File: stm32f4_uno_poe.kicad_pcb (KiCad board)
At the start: 2 copper layers, 68.6 x 53.3 mm, 94 parts, among them J104 STM32 GPIO, J106 Power, J107 Conn_01x04, J108 Ethernet, J111 Analog, J112 Barrel_Jack, J113 Conn_01x02, Q201 Si7450DP, U201 TCMT1107, U202 CJ431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

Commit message: WIP
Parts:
- removed R220: 200, Resistor_SMD:R_0402_1005Metric
- R218: footprint Resistor_SMD:R_0402_1005Metric -> Resistor_SMD:R_0603_1608Metric
- R219: value 4k7 -> 4k99; footprint Resistor_SMD:R_0402_1005Metric -> Resistor_SMD:R_0603_1608Metric
- moved R218 1.53 mm to (174.9, 83.0)
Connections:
- R219 pad 1: Net-(R219-Pad1) -> /PoE/VDD

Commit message: WIP
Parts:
- D202: value SS210 -> SS220
- D205: value 1A 200V 35ns -> 1A 1kV 75ns
- R218: value 20k -> 10k
- R219: value 4k99 -> 15k
- U201: value TCMT1107 -> EL3H7(A)(TA)-G
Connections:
- U201 pad 1: /PoE/CTL -> Net-(R201-Pad2)
- U201 pad 2: /PoE/PGND -> Net-(D201-A)
- U201 pad 3: Net-(D201-A) -> /PoE/PGND
- U201 pad 4: Net-(R201-Pad2) -> /PoE/CTL
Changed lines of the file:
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@@
     (property "Sheetfile" "poe.kicad_sch")
     (property "Sheetname" "PoE")
-    (property "isBasicPart" "NO")
+    (property "isBasicPart" "YES")
     (property "ki_description" "Diode, small symbol")
     (property "ki_keywords" "diode")
@@
     (descr "Diode SMA (DO-214AC)")
     (tags "Diode SMA (DO-214AC)")
-    (property "Description" "1V@1A 35ns Single 1A 200V SMA  Diodes - Fast Recovery Rectifiers ROHS")
-    (property "JLCPCB Part #" "C116492")
-    (property "Manufacturer" "Shandong Jingdao Microelectronics")
-    (property "Partnumber" "ES1D")
+    (property "Description" "1.7V@1A 75ns Single 1A 1kV SMA  Diodes - Fast Recovery Rectifiers ROHS")
+    (property "JLCPCB Part #" "C412437")
+    (property "Manufacturer" "MDD")
+    (property "Partnumber" "US1M")
     (property "Sheetfile" "poe.kicad_sch")
     (property "Sheetname" "PoE")
-    (property "isBasicPart" "NO")
+    (property "isBasicPart" "YES")
     (property "ki_description" "Diode, small symbol")
     (property "ki_keywords" "diode")
@@
         (effects (font (size 1 1) (thickness 0.15)))
     )
-    (fp_text value "1A 200V 35ns" (at 0 2.6) (layer "F.Fab") hide
+    (fp_text value "1A 1kV 75ns" (at 0 2.6) (layer "F.Fab") hide
         (effects (font (size 1 1) (thickness 0.15)))
     )
@@
     (descr "SOP, 4 Pin (http://www.vishay.com/docs/83510/tcmt1100.pdf), generated with kicad-footprint-generator ipc_gullwing_generator.py")
     (tags "SOP SO")
+    (property "Description" "80V 3750V 50mA 0.1V@1mA,10mA 1 6V 1.2V DC SOP-4-1.27mm  Optocouplers - Phototransistor Output ROHS")
+    (property "JLCPCB Part #" "C181879")
+    (property "Manufacturer" "Everlight Elec")
+    (property "Partnumber" "EL3H7(A)(TA)-G")
     (property "Sheetfile" "poe.kicad_sch")
     (property "Sheetname" "PoE")
+    (property "isBasicPart" "NO")
     (property "ki_description" "Optocoupler, Vce 70V, CTR 80-160%, Viso 3750V (RMS), SOP-4")
     (property "ki_keywords" "NPN DC opto")
@@
         (effects (font (size 0.8 0.8) (thickness 0.15)))
     )
-    (fp_text value "TCMT1107" (at 0 2.25) (layer "F.Fab") hide
+    (fp_text value "EL3H7(A)(TA)-G" (at 0 2.25) (layer "F.Fab") hide
         (effects (font (size 0.8 0.8) (thickness 0.15)))
     )
@@
       (stroke (width 0.1) (type solid)) (layer "F.Fab"))
     (pad "1" smd roundrect (at -3.1875 -0.635) (size 1.625 0.6) (layers "F.Cu" "F.Paste" "F.Mask") (roundrect_rratio 0.25)
-      (net 29 "/PoE/CTL") (pintype "passive"))
+      (net 50 "Net-(R201-Pad2)") (pintype "passive"))
     (pad "2" smd roundrect (at -3.1875 0.635) (size 1.625 0.6) (layers "F.Cu" "F.Paste" "F.Mask") (roundrect_rratio 0.25)
-      (net 33 "/PoE/PGND") (pintype "passive"))
-    (pad "3" smd roundrect (at 3.1875 0.635) (size 1.625 0.6) (layers "F.Cu" "F.Paste" "F.Mask") (roundrect_rratio 0.25)
       (net 35 "Net-(D201-A)") (pintype "passive"))
+    (pad "3" smd roundrect (at 3.1875 0.635) (size 1.625 0.6) (layers "F.Cu" "F.Paste" "F.Mask") (roundrect_rratio 0.25)
+      (net 33 "/PoE/PGND") (pintype "passive"))
     (pad "4" smd roundrect (at 3.1875 -0.635) (size 1.625 0.6) (layers "F.Cu" "F.Paste" "F.Mask") (roundrect_rratio 0.25)
-      (net 50 "Net-(R201-Pad2)") (pintype "passive"))
+      (net 29 "/PoE/CTL") (pintype "passive"))
     (model "${KICAD6_3DMODEL_DIR}/Package_SO.3dshapes/SOP-4_4.4x2.6mm_P1.27mm.wrl"
       (offset (xyz 0 0 0))
@@
     (property "ki_keywords" "connector")
     (attr through_hole exclude_from_bom)
-    (fp_text reference "J113" (at 0 -2.33) (layer "F.SilkS")
+    (fp_text reference "J113" (at 0 -2.33) (layer "F.SilkS") hide
         (effects (font (size 1 1) (thickness 0.15)))
     )
-    (fp_text value "Conn_01x02" (at 0 4.87) (layer "F.Fab")
+    (fp_text value "Conn_01x02" (at 0 4.87) (layer "F.Fab") hide
         (effects (font (size 1 1) (thickness 0.15)))
     )
@@
     (descr "Resistor SMD 0603 (1608 Metric), square (rectangular) end terminal, IPC_7351 nominal, (Body size source: IPC-SM-782 page 72, https://www.pcb-3d.com/wordpress/wp-content/uploads/ipc-sm-782a_amendment_1_and_2.pdf), generated with kicad-footprint-generator")
     (tags "resistor")
-    (property "Description" "100mW Thick Film Resistors ±100ppm/℃ ±1% 20kΩ 0603  Chip Resistor - Surface Mount ROHS")
-    (property "JLCPCB Part #" "C4184")
+    (property "Description" "100mW Thick Film Resistors ±100ppm/℃ ±1% 10kΩ 0603  Chip Resistor - Surface Mount ROHS")
+    (property "JLCPCB Part #" "C25804")
     (property "Manufacturer" "UNI-ROYAL(Uniroyal Elec)")
-    (property "Partnumber" "0603WAF2002T5E")
+    (property "Partnumber" "0603WAF1002T5E")
     (property "Sheetfile" "poe.kicad_sch")
     (property "Sheetname" "PoE")
@@
     (property "ki_keywords" "R resistor")
     (attr smd)
-    (fp_text reference "R218" (at 0 -1.43 180) (layer "F.SilkS")
+    (fp_text reference "R218" (at 0 -1.43 180) (layer "F.SilkS") hide
         (effects (font (size 1 1) (thickness 0.15)))
     )
-    (fp_text value "20k" (at 0 1.43 180) (layer "F.Fab")
+    (fp_text value "10k" (at 0 1.43 180) (layer "F.Fab") hide
         (effects (font (size 1 1) (thickness 0.15)))
     )
@@
     (property "ki_keywords" "DC power barrel jack connector")
     (attr through_hole exclude_from_bom)
-    (fp_text reference "J112" (at 5.75 8.45) (layer "F.SilkS")
+    (fp_text reference "J112" (at 5.75 8.45) (layer "F.SilkS") hide
         (effects (font (size 1 1) (thickness 0.15)))
     )
-    (fp_text value "Barrel_Jack" (at -5.5 6.2) (layer "F.Fab")
+    (fp_text value "Barrel_Jack" (at -5.5 6.2) (layer "F.Fab") hide
         (effects (font (size 1 1) (thickness 0.15)))
     )
@@
     (descr "SOT, 3 Pin (https://www.jedec.org/system/files/docs/to-236h.pdf variant AB), generated with kicad-footprint-generator ipc_gullwing_generator.py")
     (tags "SOT TO_SOT_SMD")
+    (property "Description" "30V Dual 200mA 0.4V@10mA SOT-23(TO-236)  Schottky Barrier Diodes (SBD) ROHS")
+    (property "JLCPCB Part #" "C7420333")
+    (property "Manufacturer" "hongjiacheng")
+    (property "Partnumber" "BAT54S")
     (property "Sheetfile" "poe.kicad_sch")
     (property "Sheetname" "PoE")
+    (property "isBasicPart" "YES")
     (property "ki_description" "Vr 30V, If 200mA, Dual schottky barrier diode, in series, SOT-323")
     (property "ki_keywords" "schottky diode")
@@
     (property "Sheetfile" "poe.kicad_sch")
     (property "Sheetname" "PoE")
-    (property "isBasicPart" "NO")
+    (property "isBasicPart" "YES")
     (property "ki_description" "Diode, small symbol")
     (property "ki_keywords" "diode")
@@
     (property "ki_keywords" "PCB Flyback Transformer")
     (attr smd)
-    (fp_text reference "TR201" (at 0 -8.255 90) (layer "F.SilkS")
+    (fp_text reference "TR201" (at 0 -8.255 90) (layer "F.SilkS") hide
         (effects (font (size 1 1) (thickness 0.15)))
     )
-    (fp_text value "Coilcraft POE40Q-xxE" (at 0.254 6.595 90) (layer "F.Fab")
+    (fp_text value "Coilcraft POE40Q-xxE" (at 0.254 6.595 90) (layer "F.Fab") hide
         (effects (font (size 1 1) (thickness 0.15)))
     )
@@
     (descr "Diode SMA (DO-214AC)")
     (tags "Diode SMA (DO-214AC)")
-    (property "Description" "100V 850mV@2A 2A SMA(DO-214AC)  Schottky Barrier Diodes (SBD) ROHS")
-    (property "JLCPCB Part #" "C14996")
+    (property "Description" "200V Single 0.95V@2.0A 2A SMA  Schottky Barrier Diodes (SBD) ROHS")
+    (property "JLCPCB Part #" "C7420361")
     (property "Manufacturer" "MDD")
-    (property "Manufacturer_Name" "MDD")
-    (property "Manufacturer_Part_Number" "SS210")
     (property "Partnumber" "SS210")
     (property "Sheetfile" "poe.kicad_sch")
@@
         (effects (font (size 0.8 0.8) (thickness 0.15)))
     )
-    (fp_text value "SS210" (at 0 2.6 90) (layer "F.Fab") hide
+    (fp_text value "SS220" (at 0 2.6 90) (layer "F.Fab") hide
         (effects (font (size 0.8 0.8) (thickness 0.15)))
     )
@@
     (descr "Resistor SMD 0603 (1608 Metric), square (rectangular) end terminal, IPC_7351 nominal, (Body size source: IPC-SM-782 page 72, https://www.pcb-3d.com/wordpress/wp-content/uploads/ipc-sm-782a_amendment_1_and_2.pdf), generated with kicad-footprint-generator")
     (tags "resistor")
-    (property "Description" "100mW Thick Film Resistors ±100ppm/℃ ±1% 4.99kΩ 0603  Chip Resistor - Surface Mount ROHS")
-    (property "JLCPCB Part #" "C23046")
+    (property "Description" "100mW Thick Film Resistors ±100ppm/℃ ±1% 15kΩ 0603  Chip Resistor - Surface Mount ROHS")
+    (property "JLCPCB Part #" "C22809")
     (property "Manufacturer" "UNI-ROYAL(Uniroyal Elec)")
-    (property "Partnumber" "0603WAF4991T5E")
+    (property "Partnumber" "0603WAF1502T5E")
     (property "Sheetfile" "poe.kicad_sch")
     (property "Sheetname" "PoE")
@@
     (property "ki_keywords" "R resistor")
     (attr smd)
-    (fp_text reference "R219" (at 0 -1.43 180) (layer "F.SilkS")
+    (fp_text reference "R219" (at 0 -1.43 180) (layer "F.SilkS") hide
         (effects (font (size 1 1) (thickness 0.15)))
     )
-    (fp_text value "4k99" (at 0 1.43 180) (layer "F.Fab")
+    (fp_text value "15k" (at 0 1.43 180) (layer "F.Fab") hide
         (effects (font (size 1 1) (thickness 0.15)))
     )

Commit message: WIP
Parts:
- removed C208, C212: 1n 2kV, Capacitor_SMD:C_1206_3216Metric
- added D209: 58V TVS, Diode_SMD:D_SMB, F.Cu at (119.0, 64.1)
- added J102: Digital/PWM, Connector_PinSocket_2.54mm:PinSocket_1x10_P2.54mm_Vertical, F.Cu at (118.8, 49.2)
- added J109: Digital/PWM, Connector_PinSocket_2.54mm:PinSocket_1x08_P2.54mm_Vertical, F.Cu at (145.7, 49.2)
- added R220: 470, Resistor_SMD:R_0402_1005Metric, F.Cu at (134.5, 57.3)
- added TP201: VDD, TestPoint:TestPoint_THTPad_2.0x2.0mm_Drill1.0mm, F.Cu at (105.5, 49.7)
- added TP202: VSS, TestPoint:TestPoint_THTPad_2.0x2.0mm_Drill1.0mm, F.Cu at (102.3, 49.7)
- D214: value 64V TVS -> 58V TVS; footprint Diode_SMD:D_SMC -> Diode_SMD:D_SMA
- L201, L202, L203, L204: value 100Ω@100MHz (800mA) -> 600Ω@100MHz (500mA)
- R215: value 1k -> 470; footprint Resistor_SMD:R_0805_2012Metric -> Resistor_SMD:R_0402_1005Metric
- R217: value 68 -> 330; footprint Resistor_SMD:R_0805_2012Metric -> Resistor_SMD:R_0402_1005Metric
- moved R231 121.6 mm to (129.6, 118.7)
- moved C219 121.0 mm to (132.9, 118.4)
- moved U204 114.0 mm to (129.6, 121.7)
- moved D207 108.3 mm to (128.7, 83.6), turned to -135 degrees
- moved R228 100.6 mm to (126.6, 87.3)
- moved D214 94.5 mm to (109.3, 51.6), turned to -90 degrees
- moved L205 93.9 mm to (116.6, 70.2)
- moved R221 90.0 mm to (116.6, 78.5), turned to 180 degrees
- moved C214 88.6 mm to (116.6, 76.3), turned to 180 degrees
- moved C207 87.0 mm to (103.7, 75.7)
- moved D205 85.6 mm to (110.4, 77.3), turned to -90 degrees
- moved C211 84.1 mm to (106.5, 68.2)
- moved R227 83.7 mm to (121.0, 88.1), turned to -90 degrees
- moved C221 79.3 mm to (142.5, 65.1)
- moved C217 79.3 mm to (142.5, 57.3)
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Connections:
- net Net-(C213-Pad1) renamed /PoE/VDD_PRI+
- net Net-(D205-A) renamed /PoE/VDD_PRI-
- net Net-(D205-K) renamed /PoE/VDD_SN
- J106 pad 8: /V_{IN} -> /PoE/24V
- R215 pad 1: /PoE/VSS -> Net-(R215-Pad1)
- R215 pad 2: Net-(U203-CLS) -> Net-(R215-Pad2)
- R217 pad 1: /PoE/VSS -> Net-(R215-Pad2)
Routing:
- net /PoE/CTL: track 0.00 -> 15.0 mm
- net /PoE/VB: track 0.00 -> 14.3 mm
- net /PoE/V_{AUX}-: track 12.2 -> 0.00 mm
- net /PoE/VDD_PRI-: track 0.00 -> 11.4 mm
- net /PoE/V_{AUX}+: track 8.04 -> 0.00 mm
- net /PoE/APD: track 0.00 -> 6.28 mm
- net /PoE/AUX: track 5.56 -> 0.00 mm
- net /PoE/FRS: track 0.00 -> 4.14 mm
- net /PoE/BLNK: track 0.00 -> 3.78 mm
- net /PoE/PGND: track 2.80 -> 0.00 mm, vias 0 -> 4
- net Net-(C202-Pad2): track 0.00 -> 1.54 mm
- net Net-(R208-Pad1): track 0.00 -> 1.49 mm
- net GND: vias 0 -> 1
- added copper zone on B.Cu, net /PoE/PGND
- added copper zone on F.Cu, net /PoE/PGND
- added copper zone on F.Cu, net GND

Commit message: WIP
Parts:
- moved R224 21.1 mm to (116.1, 70.2), turned to 90 degrees
- moved R225 19.6 mm to (114.5, 70.2), turned to 90 degrees
- moved R231 19.2 mm to (111.0, 114.0)
- moved U204 19.2 mm to (111.0, 117.0)
- moved C219 19.2 mm to (114.3, 113.7)
- moved R204 18.7 mm to (179.1, 83.1)
- moved R207 18.7 mm to (177.6, 83.1)
- moved R213 18.7 mm to (176.1, 83.1)
- moved R214 18.7 mm to (174.5, 83.1)
- moved R216 18.7 mm to (173.0, 83.1)
- moved C205 18.7 mm to (181.5, 79.8)
- moved U202 18.7 mm to (175.3, 79.8)
- moved C206 18.7 mm to (178.5, 79.8)
- moved R212 18.7 mm to (180.0, 79.8)
- moved C209 16.4 mm to (115.5, 64.1), turned to -90 degrees
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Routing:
- net /PoE/VDD: track 0.00 -> 93.8 mm, vias 0 -> 2
- net /PoE/VSS: track 0.00 -> 75.9 mm
- net Net-(Q201-S-Pad1): track 0.00 -> 41.3 mm
- net /PoE/AUX: track 0.00 -> 38.4 mm, vias 0 -> 2
- net Net-(D206-A): track 0.00 -> 36.7 mm, vias 0 -> 2
- net /PoE/VC: track 0.00 -> 36.0 mm
- net /PoE/VDD_PRI+: track 0.00 -> 30.1 mm, vias 0 -> 3
- net /PoE/V_{AUX}+: track 0.00 -> 25.6 mm
- net /PoE/CS: track 0.00 -> 19.1 mm
- net /PoE/VDD_B: track 0.00 -> 12.5 mm
- net /PoE/VSS_B: track 0.00 -> 12.4 mm
- net /PoE/VDD_PRI-: track 11.4 -> 0.00 mm, vias 0 -> 13
- net /PoE/V_{AUX}-: track 0.00 -> 10.6 mm
- net /PoE/GATE: track 0.00 -> 8.54 mm
- net /PoE/PR78: track 0.00 -> 8.18 mm
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- added copper zone on B.Cu, net /PoE/VDD_PRI+
- added copper zone on B.Cu, net /PoE/VDD_PRI-
- added copper zone on F.Cu, net /PoE/VDD_PRI-

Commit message: PCB ready
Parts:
- removed J102: Digital/PWM, Connector_PinSocket_2.54mm:PinSocket_1x10_P2.54mm_Vertical
- removed J104: STM32 GPIO, Connector_PinSocket_2.54mm:PinSocket_1x08_P2.54mm_Vertical
- removed J108: Ethernet, Connector_PinSocket_2.54mm:PinSocket_1x10_P2.54mm_Vertical
- removed J109: Digital/PWM, Connector_PinSocket_2.54mm:PinSocket_1x08_P2.54mm_Vertical
- removed J111: Analog, Connector_PinSocket_2.54mm:PinSocket_1x06_P2.54mm_Vertical
- removed R231: 10k, Resistor_SMD:R_0603_1608Metric
- removed U204: EL357N(C)(TA)-G, Package_SO:SOP-4_3.8x4.1mm_P2.54mm
- added D210: LED green, LED_SMD:LED_0603_1608Metric, F.Cu at (165.5, 77.4)
- added R232: 4k7, Resistor_SMD:R_0402_1005Metric, F.Cu at (165.4, 78.9)
- TR201: value Coilcraft POE40Q-xxE -> Coilcraft POE40Q-24E
- moved C206 35.4 mm to (150.5, 58.1)
- moved R212 35.4 mm to (152.1, 58.1)
- moved C205 35.4 mm to (153.6, 58.1), turned to 90 degrees
- moved U202 35.3 mm to (147.5, 58.1)
- moved R213 30.5 mm to (158.5, 58.1)
- moved R214 30.5 mm to (157.0, 58.1)
- moved R216 30.5 mm to (155.5, 58.1)
- moved R207 30.3 mm to (160.5, 58.1)
- moved R204 30.3 mm to (162.0, 58.1)
- moved C219 28.2 mm to (131.0, 91.0), turned to -90 degrees
- moved C225 8.81 mm to (126.8, 68.5)
- moved D201 3.94 mm to (148.6, 66.5)
- moved C201 3.68 mm to (148.6, 63.2), turned to 180 degrees
- moved R202 3.68 mm to (148.6, 61.4), turned to 180 degrees
- moved R201 3.17 mm to (148.6, 70.0)
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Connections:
- net /PoE/24V renamed /PoE/+24V
- net Net-(D208-A-Pad1) renamed /PoE/+V_SEC
- net Net-(Q201-S-Pad1) renamed /PoE/PGND_S
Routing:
- net /PoE/+24V: track 0.00 -> 94.8 mm, vias 0 -> 5
- net /PoE/T2P: track 0.00 -> 42.4 mm, vias 0 -> 2
- net /PoE/VC: track 36.0 -> 73.1 mm, vias 0 -> 3
- net Net-(D201-A): track 0.00 -> 29.8 mm
- net Net-(U202-REF): track 0.00 -> 17.7 mm
- net Net-(C222-Pad2): track 0.00 -> 4.73 mm
- net Net-(D201-COM): track 0.00 -> 4.59 mm
- net Net-(R201-Pad2): track 0.00 -> 3.40 mm
- net /PoE/VB: track 21.5 -> 23.9 mm
- net Net-(D210-A): track 0.00 -> 1.69 mm
- net Net-(C206-Pad2): track 0.00 -> 1.54 mm
- net Net-(R214-Pad2): track 0.00 -> 1.52 mm
- net Net-(R213-Pad2): track 0.00 -> 1.52 mm
- net /PoE/CTL: track 13.1 -> 14.4 mm
- net /PoE/VDD: track 93.8 -> 92.9 mm
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- added copper zone on B.Cu, net /PoE/+24V
- added copper zone on F.Cu, net /PoE/+24V
- added copper zone on B.Cu, net /PoE/+V_SEC
- added copper zone on F.Cu, net /PoE/+V_SEC

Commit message: #2 Add silkscreen texts
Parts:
- added G***: LOGO, #Logo:e-Logo 5mm, F.Cu at (142.5, 51.0)
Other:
- board text added: "+24V"
- board text added: "+3V3"
- board text added: "+5V"
- board text added: "GND"
- board text added: "PR12"
- board text added: "PR36"
- board text added: "PR45"
- board text added: "PR78"
- board text added: "VBAT"
- board text added: "VDD"
- board text added: "VSS"
- board text added: "V_{AUX}+"
- board text added: "V_{AUX}-"
- board text added: "V_{IN}"
- board text added: "easy-smart.ch STM32F4 Uno PoE"
- board text added: "easy-smart.ch STM32F4 Uno PoE ${REVISION}"
- board text added: "~{RST}"

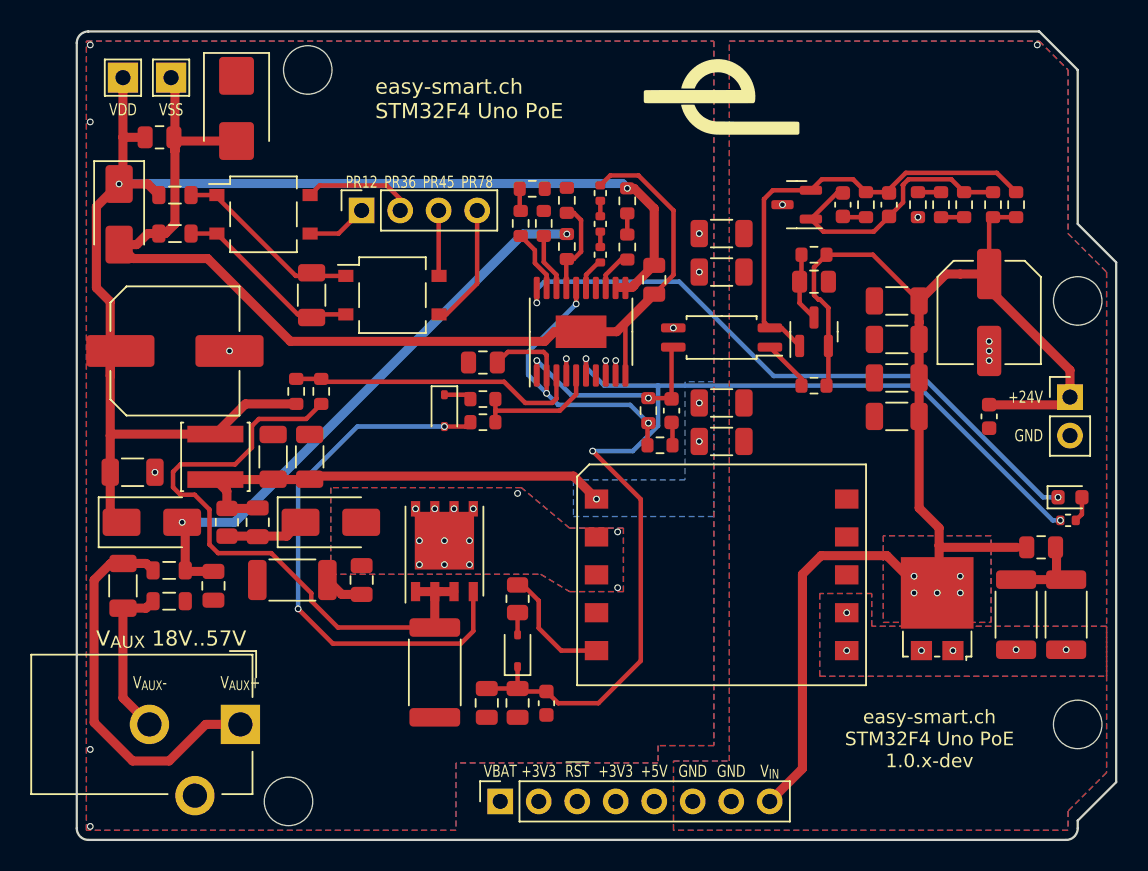
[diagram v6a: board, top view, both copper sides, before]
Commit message: Release 1.0.0 sent to JLCPCB
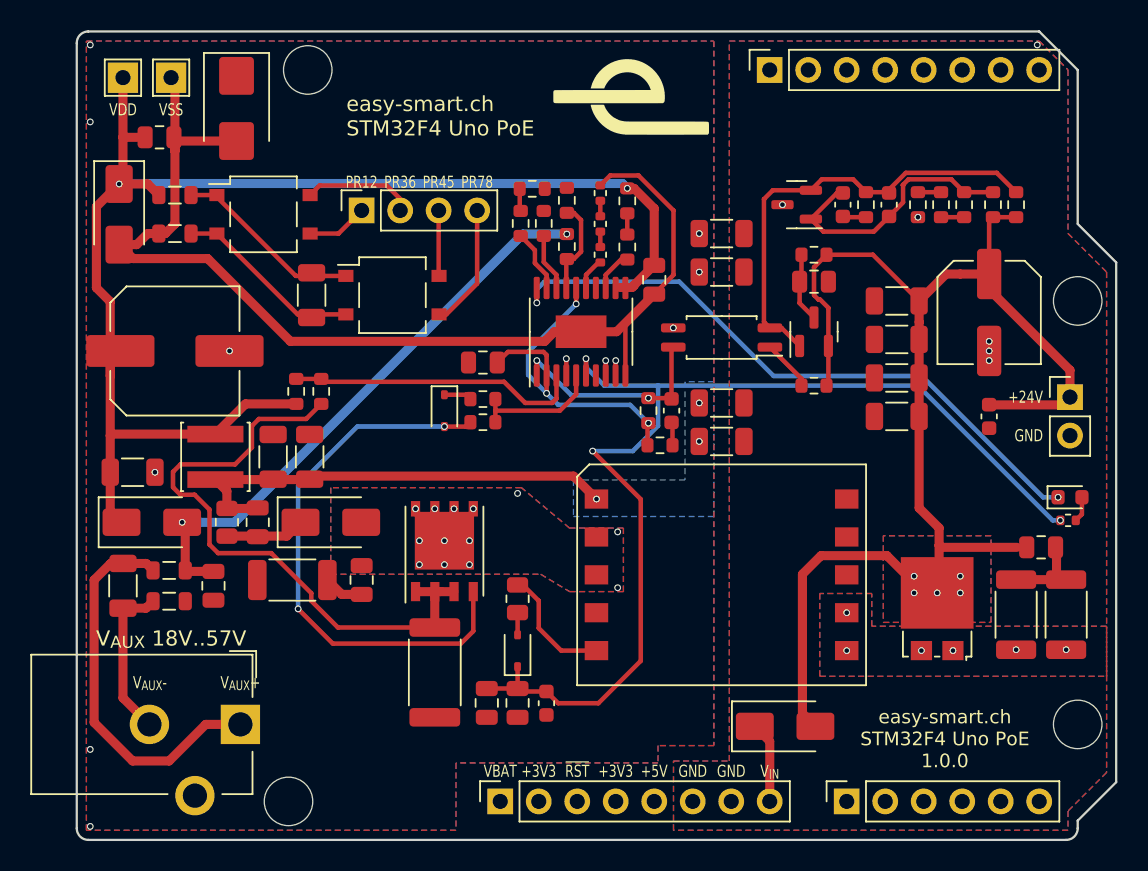
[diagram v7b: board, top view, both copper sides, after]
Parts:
- added D101: SS210, Diode_SMD:D_SMA, F.Cu at (146.7, 92.5)
- added J109: STM32 GPIO, Connector_PinSocket_2.54mm:PinSocket_1x06_P2.54mm_Vertical, F.Cu at (150.8, 97.5)
- added J110: Digital/PWM, Connector_PinSocket_2.54mm:PinSocket_1x08_P2.54mm_Vertical, F.Cu at (145.7, 49.2)
- moved G*** 5.97 mm to (136.6, 51.0)
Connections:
- J106 pad 8: /PoE/+24V -> Net-(D101-K)
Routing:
- net /PoE/+24V: track 94.8 -> 89.3 mm
- net Net-(D101-K): track 0.00 -> 5.36 mm
